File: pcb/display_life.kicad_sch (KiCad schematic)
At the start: 50 parts, among them J3 1st Bit_shifter, J4 1st 7 Segment, J5 2nd Bit_shifter, J6 2nd 7 Segment, J7 decoder_input, J8 disp_1_decoder, J9 disp_2_decoder, Q1 Q_NPN_CBE, Q2 Q_NPN_CBE, Q3 Q_NPN_CBE, Q4 Q_NPN_CBE, Q5 Q_NPN_CBE, Q6 Q_NPN_CBE, Q7 Q_NPN_CBE, Q8 Q_NPN_CBE, U2 74HC595, U3 74HC595, U4 4028, U5 CC56-12SURKWA, U6 CC56-12SURKWA

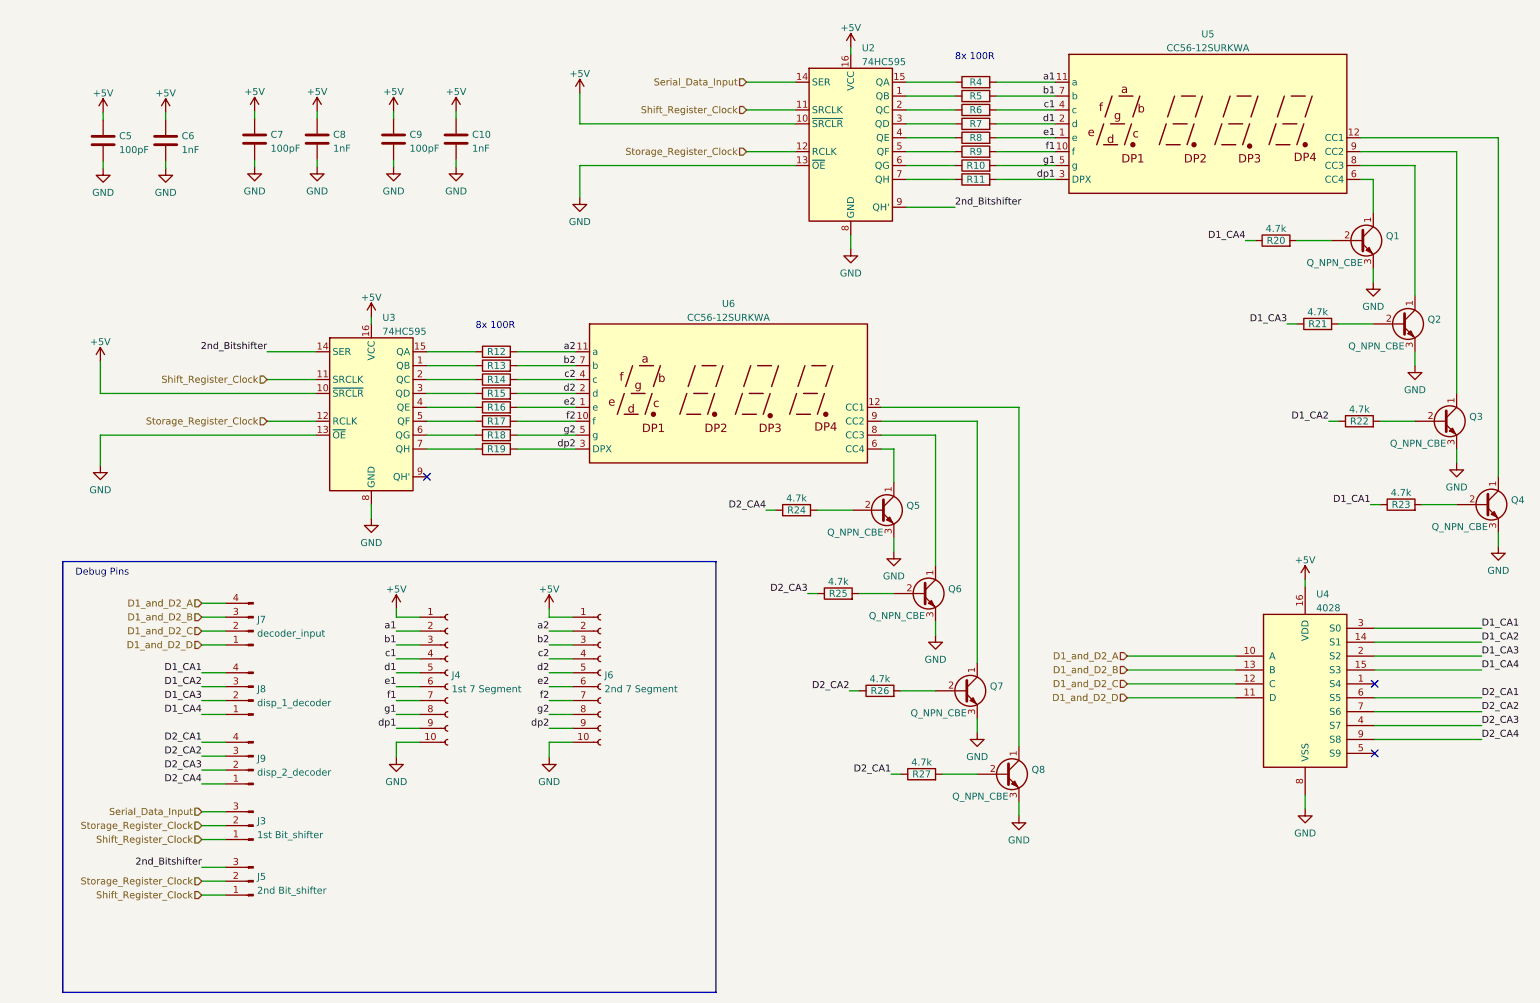
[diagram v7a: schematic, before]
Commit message: pulldown to signals
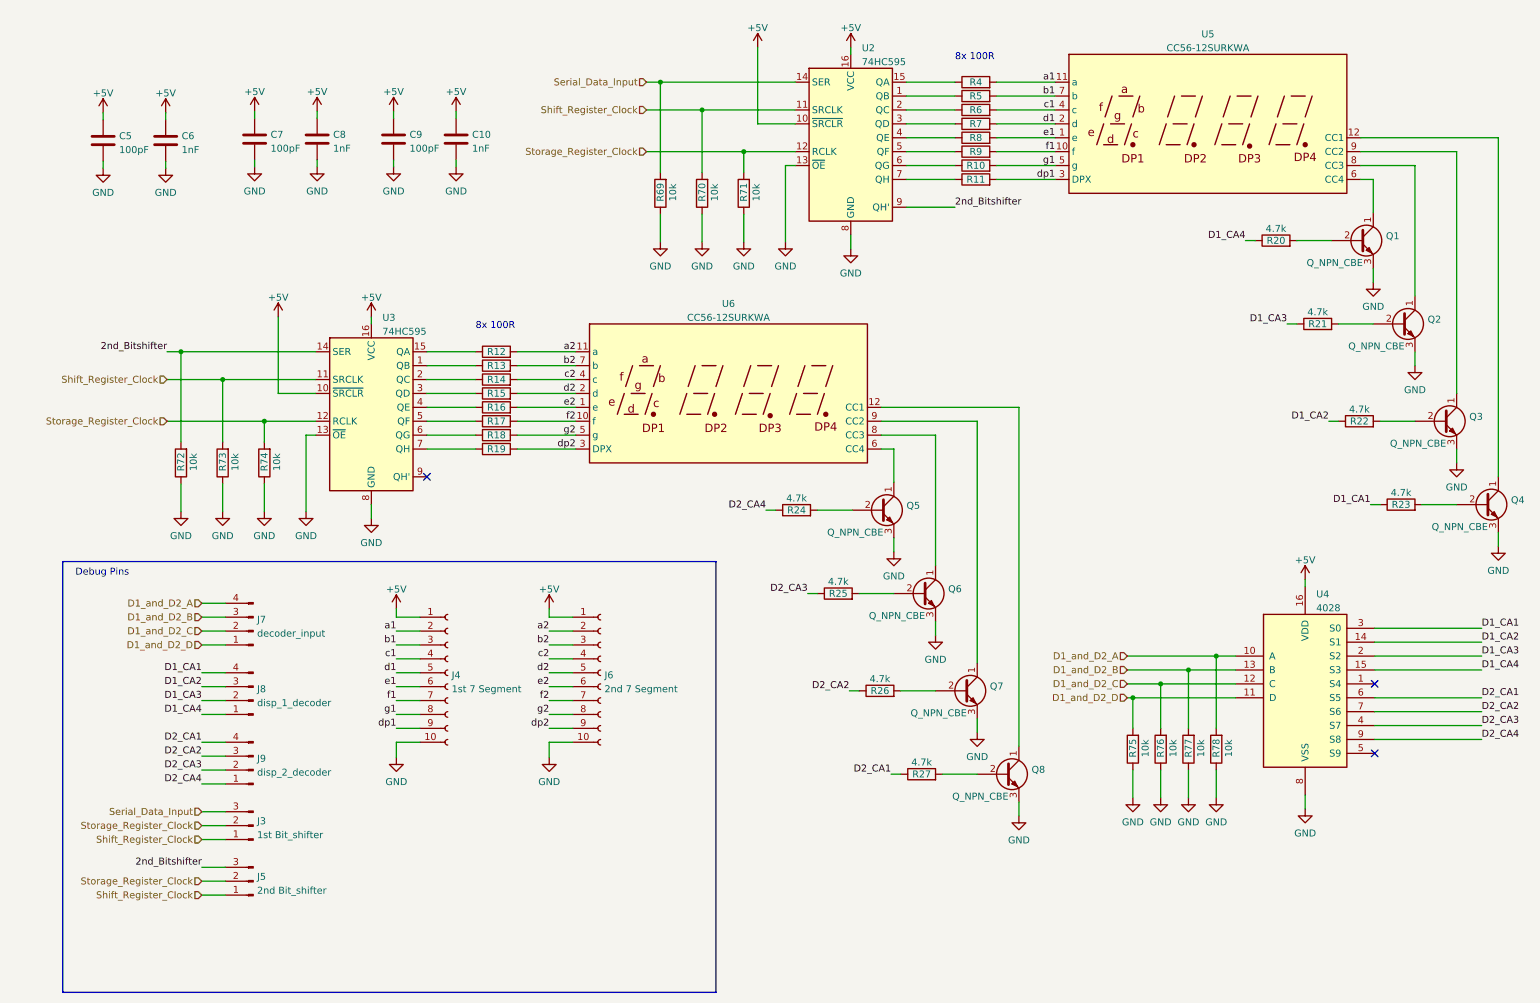
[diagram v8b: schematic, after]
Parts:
- added R69, R70, R71, R72, R73, R74, R75, R76, R77, R78: 10k, Resistor_THT:R_Axial_DIN0207_L6.3mm_D2.5mm_P10.16mm_Horizontal, symbol Device:R
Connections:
- net 2nd_Bitshifter: now also R72.2
- net D1_and_D2_A: now also R78.2
- net D1_and_D2_B: now also R77.2
- net D1_and_D2_C: now also R76.2
- net D1_and_D2_D: now also R75.2
- net GND: now also R69.1, R70.1, R71.1, R72.1, R73.1, R74.1, R75.1, R76.1, R77.1, R78.1
- net Serial_Data_Input: now also R69.2
- net Shift_Register_Clock: now also R70.2, R73.2
- net Storage_Register_Clock: now also R71.2, R74.2
